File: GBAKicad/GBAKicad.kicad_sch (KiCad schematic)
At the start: 60 parts, among them J1 USB_C_Receptacle_USB2.0_16P, J2 Micro_SD_Card_Det1, J3 AudioJack3_SwitchT, SW1 SW_Push, SW10 SW_Push, SW11 SW_SPDT, SW2 SW_Push, SW3 SW_Push, SW4 SW_Push, SW5 SW_Push, SW6 SW_Push, SW7 SW_Push, SW8 SW_Push, SW9 SW_Push, U1 TFT_320x240, U2 XC6220B331MR, U3 TP4056-42-ESOP8, U4 MAX17048, U5 PCM5102A, U6 TPA2012D2RTJR, U7 ESP32-S3

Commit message: schemtics
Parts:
- removed C1, C2, C3, C4, C5, C6, C7, C8: 100nF, symbol Device:C
- removed C9: 1uF, symbol Device:C
- added C13, C14: 2.2uF, symbol Device:C
- added C15, C16, C17, C18, C19, C20, C21, C22, C24, C25: 100nF, symbol Device:C
- added C23: 1uF, symbol Device:C
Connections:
- net +3V3: now also C15.1, C16.1, C17.1, C18.1, C19.1, C20.2, C21.1, C22.2, C23.2; no longer U1.1 (VCC), U2.3 (CE), U2.5 (VOUT), U4.3 (VDD), U5.20 (DVDD), U5.8 (AVDD), U6.13 (PVDD), U6.3 (PVDD), U7.2 (VDD3P3), U7.20 (VDD3P3_RTC), U7.3 (VDD3P3), U7.46 (VDD3P3_CPU)
- net GND: now also C13.2, C14.2
- net VBAT: now also U2.3 (CE)
- net VBUS: now also C24.2, C25.1; no longer J1.A4 (VBUS), J1.A9 (VBUS), J1.B4 (VBUS), J1.B9 (VBUS), U3.4 (V_{CC})
- net at U5.18 (LDOO): now also C13.1
- net at U5.5 (VNEG): now also C14.1
- new net: C23.1, U2.5 (VOUT)
- new net: C21.2, U4.3 (VDD)
- new net: C22.1, U1.1 (VCC)
- new net: C18.2, U5.20 (DVDD)
- new net: C25.2, U3.4 (V_{CC})
- new net: C19.2, U5.8 (AVDD)
- new net: C24.1, J1.A4 (VBUS), J1.A9 (VBUS), J1.B4 (VBUS), J1.B9 (VBUS)
- new net: C17.2, U7.46 (VDD3P3_CPU)
- new net: C16.2, U7.20 (VDD3P3_RTC)
- new net: C15.2, U7.2 (VDD3P3), U7.3 (VDD3P3)
- new net PVDD: C20.1, U6.13 (PVDD), U6.3 (PVDD)
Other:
- moved on the sheet: BT1, C10, C11, C12, J1, J2, J3, LS1, R1, R10, R13, R14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

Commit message: schematics finshed???
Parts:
- removed C10, C11: 100nF, symbol Device:C
- added C26, C27: 100nF, Capacitor_SMD:C_0402_1005Metric, symbol Device:C
- BT1: footprint (none) -> Connector_JST:JST_PH_B2B-PH-K_1x02_P2.00mm_Vertical
- C12, C15, C16, C17, C18, C19, C20, C21, C22, C23, C24, C25: footprint (none) -> Capacitor_SMD:C_0402_1005Metric
- C13, C14: footprint (none) -> Capacitor_SMD:C_0201_0603Metric
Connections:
- net +3V3: now also C26.1, C27.1; no longer U7.29 (VDD_SPI), U7.55 (VDDA), U7.56 (VDDA)
- new net: C26.2, U7.55 (VDDA), U7.56 (VDDA)
- new net: C27.2, U7.29 (VDD_SPI)

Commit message: schemtics asign fotpitn pt 1
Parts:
- J1: footprint (none) -> Connector_USB:USB_C_Receptacle_HRO_TYPE-C-31-M-12
- J2: footprint (none) -> Connector_Card:microSD_HC_Hirose_DM3AT-SF-PEJM5
- J3: footprint (none) -> Connector_Audio:Jack_3.5mm_QingPu_WQP-PJ398SM_Vertical_CircularHoles
- LS1: footprint (none) -> Connector_JST:JST_PH_B2B-PH-K_1x02_P2.00mm_Vertical
- R1, R10, R11, R12, R13, R14, R15, R2, R3, R4, R5, R6, R7, R8, R9: footprint (none) -> Resistor_SMD:R_0402_1005Metric
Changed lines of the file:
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@@
 			)
 		)
-		(property "Footprint" ""
+		(property "Footprint" "Resistor_SMD:R_0402_1005Metric"
 			(at 222.25 244.602 90)
 			(hide yes)
@@
 			)
 		)
-		(property "Footprint" ""
+		(property "Footprint" "Resistor_SMD:R_0402_1005Metric"
 			(at 84.582 185.42 90)
 			(hide yes)
@@
 			)
 		)
-		(property "Footprint" ""
+		(property "Footprint" "Resistor_SMD:R_0402_1005Metric"
 			(at 304.8 94.488 90)
 			(hide yes)
@@
 			)
 		)
-		(property "Footprint" ""
+		(property "Footprint" "Resistor_SMD:R_0402_1005Metric"
 			(at 36.322 146.05 90)
 			(hide yes)
@@
 			)
 		)
-		(property "Footprint" ""
+		(property "Footprint" "Resistor_SMD:R_0402_1005Metric"
 			(at 304.8 76.708 90)
 			(hide yes)
@@
 			)
 		)
-		(property "Footprint" ""
+		(property "Footprint" "Resistor_SMD:R_0402_1005Metric"
 			(at 127.762 185.42 90)
 			(hide yes)
@@
 			)
 		)
-		(property "Footprint" ""
+		(property "Footprint" "Resistor_SMD:R_0402_1005Metric"
 			(at 127.762 146.05 90)
 			(hide yes)
@@
 			)
 		)
-		(property "Footprint" ""
+		(property "Footprint" "Resistor_SMD:R_0402_1005Metric"
 			(at 84.582 146.05 90)
 			(hide yes)
@@
 			)
 		)
-		(property "Footprint" ""
+		(property "Footprint" "Resistor_SMD:R_0402_1005Metric"
 			(at 389.89 178.562 90)
 			(hide yes)
@@
 			)
 		)
-		(property "Footprint" ""
+		(property "Footprint" "Resistor_SMD:R_0402_1005Metric"
 			(at 106.172 146.05 90)
 			(hide yes)
@@
 			)
 		)
-		(property "Footprint" ""
+		(property "Footprint" "Resistor_SMD:R_0402_1005Metric"
 			(at 106.172 185.42 90)
 			(hide yes)
@@
 			)
 		)
-		(property "Footprint" ""
+		(property "Footprint" "Connector_Audio:Jack_3.5mm_QingPu_WQP-PJ398SM_Vertical_CircularHoles"
 			(at 381 168.91 0)
 			(hide yes)
@@
 			)
 		)
-		(property "Footprint" ""
+		(property "Footprint" "Resistor_SMD:R_0402_1005Metric"
 			(at 36.322 185.42 90)
 			(hide yes)
@@
 			)
 		)
-		(property "Footprint" ""
+		(property "Footprint" "Resistor_SMD:R_0402_1005Metric"
 			(at 60.452 146.05 90)
 			(hide yes)
@@
 			)
 		)
-		(property "Footprint" ""
+		(property "Footprint" "Connector_JST:JST_PH_B2B-PH-K_1x02_P2.00mm_Vertical"
 			(at 361.95 180.34 0)
 			(hide yes)
@@
 			)
 		)
-		(property "Footprint" ""
+		(property "Footprint" "Resistor_SMD:R_0402_1005Metric"
 			(at 60.452 185.42 90)
 			(hide yes)
@@
 			)
 		)
-		(property "Footprint" ""
+		(property "Footprint" "Connector_Card:microSD_HC_Hirose_DM3AT-SF-PEJM5"
 			(at 387.35 67.31 0)
 			(hide yes)
@@
 			)
 		)
-		(property "Footprint" ""
+		(property "Footprint" "Resistor_SMD:R_0402_1005Metric"
 			(at 222.25 242.062 90)
 			(hide yes)
@@
 			)
 		)
-		(property "Footprint" ""
+		(property "Footprint" "Connector_USB:USB_C_Receptacle_HRO_TYPE-C-31-M-12"
 			(at 102.87 54.61 0)
 			(hide yes)

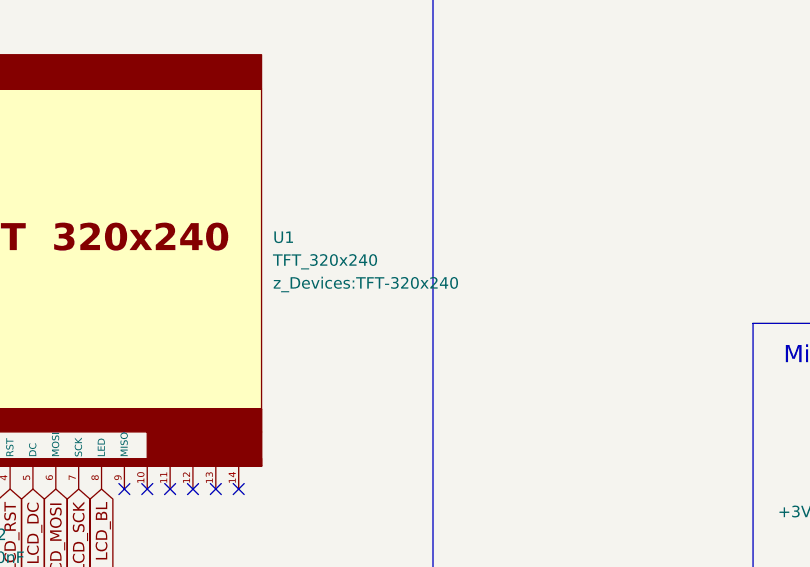
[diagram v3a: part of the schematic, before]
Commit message: schemtic assgining footpritns
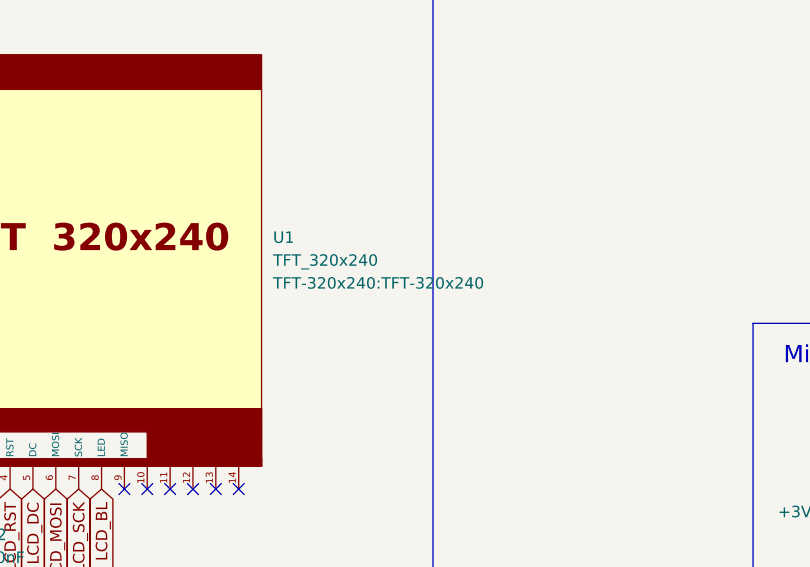
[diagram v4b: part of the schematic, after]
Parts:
- C12, C15, C16, C17, C18, C19, C20, C21, C22, C23, C24, C25, C26, C27: footprint Capacitor_SMD:C_0402_1005Metric -> Capacitor_SMD:C_0603_1608Metric
- C13, C14: footprint Capacitor_SMD:C_0201_0603Metric -> Capacitor_SMD:C_0603_1608Metric
- R1, R10, R11, R12, R13, R14, R15, R2, R3, R4, R5, R6, R7, R8, R9: footprint Resistor_SMD:R_0402_1005Metric -> Resistor_SMD:R_0603_1608Metric
- R16, R17, R18, R19, R20, R21, R22, R23, R24, R25: footprint (none) -> Resistor_SMD:R_0603_1608Metric
- SW1, SW10, SW2, SW3, SW4, SW5, SW6, SW7, SW8, SW9: footprint (none) -> Button_Switch_THT:SW_PUSH_6mm_H5mm
- SW11: footprint (none) -> Connector_PinHeader_2.54mm:PinHeader_1x14_P2.54mm_Vertical
- U1: footprint z_Devices:TFT-320x240 -> TFT-320x240:TFT-320x240
- U7: footprint Package_DFN_QFN:QFN-56-1EP_7x7mm_P0.4mm_EP4x4mm -> RF_Module:ESP32-S3-WROOM-1
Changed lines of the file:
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@@
 			)
 		)
-		(property "Footprint" "Capacitor_SMD:C_0402_1005Metric"
+		(property "Footprint" "Capacitor_SMD:C_0603_1608Metric"
 			(at 175.26 237.7948 0)
 			(hide yes)
@@
 			)
 		)
-		(property "Footprint" ""
+		(property "Footprint" "Button_Switch_THT:SW_PUSH_6mm_H5mm"
 			(at 91.44 157.48 0)
 			(hide yes)
@@
 			)
 		)
-		(property "Footprint" ""
+		(property "Footprint" "Button_Switch_THT:SW_PUSH_6mm_H5mm"
 			(at 67.31 157.48 0)
 			(hide yes)
@@
 			)
 		)
-		(property "Footprint" "Resistor_SMD:R_0402_1005Metric"
+		(property "Footprint" "Resistor_SMD:R_0603_1608Metric"
 			(at 222.25 244.602 90)
 			(hide yes)
@@
 			)
 		)
-		(property "Footprint" ""
+		(property "Footprint" "Resistor_SMD:R_0603_1608Metric"
 			(at 119.38 45.212 90)
 			(hide yes)
@@
 			)
 		)
-		(property "Footprint" ""
+		(property "Footprint" "Button_Switch_THT:SW_PUSH_6mm_H5mm"
 			(at 113.03 157.48 0)
 			(hide yes)
@@
 			)
 		)
-		(property "Footprint" "Resistor_SMD:R_0402_1005Metric"
+		(property "Footprint" "Resistor_SMD:R_0603_1608Metric"
 			(at 84.582 185.42 90)
 			(hide yes)
@@
 			)
 		)
-		(property "Footprint" "Resistor_SMD:R_0402_1005Metric"
+		(property "Footprint" "Resistor_SMD:R_0603_1608Metric"
 			(at 304.8 94.488 90)
 			(hide yes)
@@
 			)
 		)
-		(property "Footprint" ""
+		(property "Footprint" "Resistor_SMD:R_0603_1608Metric"
 			(at 226.06 169.418 90)
 			(hide yes)
@@
 			)
 		)
-		(property "Footprint" "Resistor_SMD:R_0402_1005Metric"
+		(property "Footprint" "Resistor_SMD:R_0603_1608Metric"
 			(at 36.322 146.05 90)
 			(hide yes)
@@
 			)
 		)
-		(property "Footprint" "Resistor_SMD:R_0402_1005Metric"
+		(property "Footprint" "Resistor_SMD:R_0603_1608Metric"
 			(at 304.8 76.708 90)
 			(hide yes)
@@
 			)
 		)
-		(property "Footprint" "Capacitor_SMD:C_0402_1005Metric"
+		(property "Footprint" "Capacitor_SMD:C_0603_1608Metric"
 			(at 192.7352 82.55 0)
 			(hide yes)
@@
 			)
 		)
-		(property "Footprint" ""
+		(property "Footprint" "Resistor_SMD:R_0603_1608Metric"
 			(at 170.18 141.478 90)
 			(hide yes)
@@
 			)
 		)
-		(property "Footprint" "Resistor_SMD:R_0402_1005Metric"
+		(property "Footprint" "Resistor_SMD:R_0603_1608Metric"
 			(at 127.762 185.42 90)
 			(hide yes)
@@
 			)
 		)
-		(property "Footprint" "Capacitor_SMD:C_0402_1005Metric"
+		(property "Footprint" "Capacitor_SMD:C_0603_1608Metric"
 			(at 272.7452 144.78 0)
 			(hide yes)
@@
 			)
 		)
-		(property "Footprint" "Capacitor_SMD:C_0402_1005Metric"
+		(property "Footprint" "Capacitor_SMD:C_0603_1608Metric"
 			(at 207.9752 228.6 0)
 			(hide yes)
@@
 			)
 		)
-		(property "Footprint" "Resistor_SMD:R_0402_1005Metric"
+		(property "Footprint" "Resistor_SMD:R_0603_1608Metric"
 			(at 127.762 146.05 90)
 			(hide yes)
@@
 			)
 		)
-		(property "Footprint" "Resistor_SMD:R_0402_1005Metric"
+		(property "Footprint" "Resistor_SMD:R_0603_1608Metric"
 			(at 84.582 146.05 90)
 			(hide yes)
@@
 			)
 		)
-		(property "Footprint" "Capacitor_SMD:C_0402_1005Metric"
+		(property "Footprint" "Capacitor_SMD:C_0603_1608Metric"
 			(at 275.2852 151.13 0)
 			(hide yes)
@@
 			)
 		)
-		(property "Footprint" ""
+		(property "Footprint" "Resistor_SMD:R_0603_1608Metric"
 			(at 191.77 245.618 90)
 			(hide yes)
@@
 			)
 		)
-		(property "Footprint" ""
+		(property "Footprint" "Resistor_SMD:R_0603_1608Metric"
 			(at 226.06 196.342 90)
 			(hide yes)
@@
 			)
 		)
-		(property "Footprint" "Resistor_SMD:R_0402_1005Metric"
+		(property "Footprint" "Resistor_SMD:R_0603_1608Metric"
 			(at 389.89 178.562 90)
 			(hide yes)
@@
 			)
 		)
-		(property "Footprint" ""
+		(property "Footprint" "Button_Switch_THT:SW_PUSH_6mm_H5mm"
 			(at 67.31 196.85 0)
 			(hide yes)
@@
 			)
 		)
-		(property "Footprint" "Resistor_SMD:R_0402_1005Metric"
+		(property "Footprint" "Resistor_SMD:R_0603_1608Metric"
 			(at 106.172 146.05 90)
 			(hide yes)
@@
 			)
 		)
-		(property "Footprint" "Resistor_SMD:R_0402_1005Metric"
+		(property "Footprint" "Resistor_SMD:R_0603_1608Metric"
 			(at 106.172 185.42 90)
 			(hide yes)
@@
 			)
 		)
-		(property "Footprint" "Capacitor_SMD:C_0402_1005Metric"
+		(property "Footprint" "Capacitor_SMD:C_0603_1608Metric"
 			(at 123.19 38.4048 0)
 			(hide yes)
@@
 			)
 		)
-		(property "Footprint" "Capacitor_SMD:C_0402_1005Metric"
+		(property "Footprint" "Capacitor_SMD:C_0603_1608Metric"
 			(at 358.14 161.5948 0)
 			(hide yes)
@@
 			)
 		)
-		(property "Footprint" ""
+		(property "Footprint" "Connector_PinHeader_2.54mm:PinHeader_1x14_P2.54mm_Vertical"
 			(at 229.87 266.7 0)
 			(hide yes)
@@
 			)
 		)
-		(property "Footprint" ""
+		(property "Footprint" "Button_Switch_THT:SW_PUSH_6mm_H5mm"
 			(at 134.62 196.85 0)
 			(hide yes)
@@
 			)
 		)
-		(property "Footprint" "Resistor_SMD:R_0402_1005Metric"
+		(property "Footprint" "Resistor_SMD:R_0603_1608Metric"
 			(at 36.322 185.42 90)
 			(hide yes)
@@
 			)
 		)
-		(property "Footprint" ""
+		(property "Footprint" "Button_Switch_THT:SW_PUSH_6mm_H5mm"
 			(at 113.03 196.85 0)
 			(hide yes)
@@
 			)
 		)
-		(property "Footprint" "Resistor_SMD:R_0402_1005Metric"
+		(property "Footprint" "Resistor_SMD:R_0603_1608Metric"
 			(at 60.452 146.05 90)
 			(hide yes)
@@
 			)
 		)
-		(property "Footprint" ""
+		(property "Footprint" "Resistor_SMD:R_0603_1608Metric"
 			(at 297.18 239.522 90)
 			(hide yes)
@@
 			)
 		)
-		(property "Footprint" "Capacitor_SMD:C_0402_1005Metric"
+		(property "Footprint" "Capacitor_SMD:C_0603_1608Metric"
 			(at 204.1652 130.81 0)
 			(hide yes)
@@
 			)
 		)
-		(property "Footprint" "Capacitor_SMD:C_0402_1005Metric"
+		(property "Footprint" "Capacitor_SMD:C_0603_1608Metric"
 			(at 194.0052 130.81 0)
 			(hide yes)
@@
 			)
 		)
-		(property "Footprint" ""
+		(property "Footprint" "Resistor_SMD:R_0603_1608Metric"
 			(at 271.78 234.442 90)
 			(hide yes)
@@
 			)
 		)
-		(property "Footprint" "Capacitor_SMD:C_0402_1005Metric"
+		(property "Footprint" "Capacitor_SMD:C_0603_1608Metric"
 			(at 247.65 235.2548 0)
 			(hide yes)
@@
 			)
 		)
-		(property "Footprint" "Capacitor_SMD:C_0402_1005Metric"
+		(property "Footprint" "Capacitor_SMD:C_0603_1608Metric"
 			(at 199.0852 129.54 0)
 			(hide yes)
@@
 			)
 		)
-		(property "Footprint" ""
+		(property "Footprint" "Resistor_SMD:R_0603_1608Metric"
 			(at 191.77 248.158 90)
 			(hide yes)
@@
 			)
 		)
-		(property "Footprint" "Resistor_SMD:R_0402_1005Metric"
+		(property "Footprint" "Resistor_SMD:R_0603_1608Metric"
 			(at 60.452 185.42 90)
 			(hide yes)
@@
 			)
 		)
-		(property "Footprint" "Capacitor_SMD:C_0402_1005Metric"
+		(property "Footprint" "Capacitor_SMD:C_0603_1608Metric"
 			(at 196.5452 124.46 0)
 			(hide yes)
@@
 			)
 		)
-		(property "Footprint" ""
+		(property "Footprint" "Button_Switch_THT:SW_PUSH_6mm_H5mm"
 			(at 91.44 196.85 0)
 			(hide yes)
@@
 			)
 		)
-		(property "Footprint" "Capacitor_SMD:C_0402_1005Metric"
+		(property "Footprint" "Capacitor_SMD:C_0603_1608Metric"
 			(at 286.7152 177.8 0)
 			(hide yes)
@@
 			)
 		)
-		(property "Footprint" ""
+		(property "Footprint" "Button_Switch_THT:SW_PUSH_6mm_H5mm"
 			(at 43.18 157.48 0)
 			(hide yes)
@@
 			)
 		)
-		(property "Footprint" "Package_DFN_QFN:QFN-56-1EP_7x7mm_P0.4mm_EP4x4mm"
+		(property "Footprint" "RF_Module:ESP32-S3-WROOM-1"
 			(at 198.12 218.44 0)
 			(hide yes)
@@
 			)
 		)
-		(property "Footprint" "Capacitor_SMD:C_0201_0603Metric"
+		(property "Footprint" "Capacitor_SMD:C_0603_1608Metric"
 			(at 302.26 181.9148 0)
 			(hide yes)
@@
 			)
 		)
-		(property "Footprint" "Capacitor_SMD:C_0402_1005Metric"
+		(property "Footprint" "Capacitor_SMD:C_0603_1608Metric"
 			(at 201.6252 116.84 0)
 			(hide yes)
@@
 			)
 		)
-		(property "Footprint" "Resistor_SMD:R_0402_1005Metric"
+		(property "Footprint" "Resistor_SMD:R_0603_1608Metric"
 			(at 222.25 242.062 90)
 			(hide yes)
@@
 			)
 		)
-		(property "Footprint" ""
+		(property "Footprint" "Button_Switch_THT:SW_PUSH_6mm_H5mm"
 			(at 43.18 196.85 0)
 			(hide yes)
@@
 			)
 		)
-		(property "Footprint" ""
+		(property "Footprint" "Button_Switch_THT:SW_PUSH_6mm_H5mm"
 			(at 134.62 157.48 0)
 			(hide yes)
@@
 			)
 		)
-		(property "Footprint" ""
+		(property "Footprint" "Resistor_SMD:R_0603_1608Metric"
 			(at 297.18 242.062 90)
 			(hide yes)
@@
 			)
 		)
-		(property "Footprint" ""
+		(property "Footprint" "Resistor_SMD:R_0603_1608Metric"
 			(at 119.38 42.672 90)
 			(hide yes)
@@
 			)
 		)
-		(property "Footprint" "z_Devices:TFT-320x240"
+		(property "Footprint" "TFT-320x240:TFT-320x240"
 			(at 228.6 49.5299 0)
 			(show_name no)
@@
 			)
 		)
-		(property "Footprint" "Capacitor_SMD:C_0201_0603Metric"
+		(property "Footprint" "Capacitor_SMD:C_0603_1608Metric"
 			(at 293.37 184.4548 0)
 			(hide yes)

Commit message: Schematics done!
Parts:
- removed BT1: Battery, Connector_JST:JST_PH_B2B-PH-K_1x02_P2.00mm_Vertical, symbol Device:Battery
- removed C12, C23: 1uF, Capacitor_SMD:C_0603_1608Metric, symbol Device:C
- removed C14: 2.2uF, Capacitor_SMD:C_0603_1608Metric, symbol Device:C
- removed C15, C16, C17, C18, C19, C20, C21, C22, C24, C25, C26, C27: 100nF, Capacitor_SMD:C_0603_1608Metric, symbol Device:C
- removed J2: Micro_SD_Card_Det1, Connector_Card:microSD_HC_Hirose_DM3AT-SF-PEJM5, symbol Connector:Micro_SD_Card_Det1
- removed J3: AudioJack3_SwitchT, Connector_Audio:Jack_3.5mm_QingPu_WQP-PJ398SM_Vertical_CircularHoles, symbol Connector_Audio:AudioJack3_SwitchT
- removed LS1: Speaker, Connector_JST:JST_PH_B2B-PH-K_1x02_P2.00mm_Vertical, symbol Device:Speaker
- removed R18, R21, R23: 10k, Resistor_SMD:R_0603_1608Metric, symbol Device:R
- removed R19, R20: 4.7k, Resistor_SMD:R_0603_1608Metric, symbol Device:R
- removed R22, R25: 5.1k, Resistor_SMD:R_0603_1608Metric, symbol Device:R
- removed R24: 100, Resistor_SMD:R_0603_1608Metric, symbol Device:R
- removed SW11: SW_SPDT, Connector_PinHeader_2.54mm:PinHeader_1x14_P2.54mm_Vertical, symbol Switch:SW_SPDT
- removed SW2: SW_Push, Button_Switch_THT:SW_PUSH_6mm_H5mm, symbol Switch:SW_Push
- removed U1: TFT_320x240, TFT-320x240:TFT-320x240, symbol tft_320x240:TFT_320x240
- removed U2: XC6220B331MR, Package_TO_SOT_SMD:SOT-23-5, symbol Regulator_Linear:XC6220B331MR
- removed U4: MAX17048, Package_DFN_QFN:DFN-8-1EP_2x2mm_P0.5mm_EP0.7x1.3mm, symbol PCM_marbastlib-various:MAX17048
- removed U5: PCM5102A, Package_SO:TSSOP-20_4.4x6.5mm_P0.65mm, symbol Audio:PCM5102A
- removed U6: TPA2012D2RTJR, TPA2012D2RTJR:QFN50P400X400X80-21N270X270, symbol TPA2012D2RTJR:TPA2012D2RTJR
- removed U7: ESP32-S3, RF_Module:ESP32-S3-WROOM-1, symbol MCU_Espressif:ESP32-S3
- added C1, C3: 100nF, Capacitor_SMD:C_0603_1608Metric, symbol Device:C
- added C10, C4, C5, C6: 10uF, Capacitor_SMD:C_0603_1608Metric, symbol Device:C
- added C11: 10uF, Capacitor_Tantalum_SMD:CP_EIA-3216-18_Kemet-A, symbol Device:C_Polarized
- added C12: 22uF, Capacitor_Tantalum_SMD:CP_EIA-3216-18_Kemet-A, symbol Device:C_Polarized
- added C2: 22nF, Capacitor_SMD:C_0603_1608Metric, symbol Device:C
- added C7, C8, C9: 100uF, Capacitor_SMD:C_0603_1608Metric, symbol Device:C
- added D1: RED, LED_SMD:LED_0603_1608Metric, symbol Device:LED
- added D2: BLUE, LED_SMD:LED_0603_1608Metric, symbol Device:LED
- added J2: BATT_Conn, symbol Connector:Conn_01x02_Socket
- added J3: Jumper, symbol Jumper:SolderJumper_2_Open
- added J4: OLED_Conn, symbol Connector:Conn_01x04_Socket
- added Q1: (no value), Custom Footprints:SOT-23-6L_TCP, symbol DIY_symbols:FS8205A
- added Q2: PMOS, symbol Simulation_SPICE:PMOS
- added SW11, SW12, SW13, SW14, SW15: SW_Push, symbol Switch:SW_Push
- added SW16: BTN_SYS, symbol Switch:SW_Push
- added SW2: SW_SPDT, symbol Switch:SW_SPDT
- added TP1, TP3, TP5: TestPoint, symbol Connector:TestPoint
- added TP4: AMS_3V3, symbol Connector:TestPoint
- added U1: ESP32-S3-WROOM-1, RF_Module:ESP32-S3-WROOM-1, symbol RF_Module:ESP32-S3-WROOM-1
- added U2: MIC5219-3.3YM5, Package_TO_SOT_SMD:SOT-23-5, symbol Regulator_Linear:MIC5219-3.3YM5
- added U4: DW01A, Package_TO_SOT_SMD:SOT-23-6, symbol Battery_Management:DW01A
- added U5: AMS1117-3.3, Package_TO_SOT_SMD:SOT-223-3_TabPin2, symbol Regulator_Linear:AMS1117-3.3
- C13: value 2.2uF -> 100nF
- J1: footprint Connector_USB:USB_C_Receptacle_HRO_TYPE-C-31-M-12 -> Connector_USB:USB_C_Receptacle_GCT_USB4105-xx-A_16P_TopMnt_Horizontal
- R1, R17: footprint Resistor_SMD:R_0603_1608Metric -> (none)
- R10, R11, R12, R13, R15, R16: value 10k -> 100k; footprint Resistor_SMD:R_0603_1608Metric -> (none)
- R14: value 1.2k -> 100k; footprint Resistor_SMD:R_0603_1608Metric -> (none)
- R2, R3: value 10k -> 5.1k; footprint Resistor_SMD:R_0603_1608Metric -> (none)
- R4: value 10k -> 1.2k; footprint Resistor_SMD:R_0603_1608Metric -> (none)
- R5, R6, R7: value 10k -> 1k; footprint Resistor_SMD:R_0603_1608Metric -> (none)
- R8, R9: value 10k -> 100R; footprint Resistor_SMD:R_0603_1608Metric -> (none)
- SW1: value SW_Push -> EN; footprint Button_Switch_THT:SW_PUSH_6mm_H5mm -> (none)
- SW10, SW4, SW5, SW6, SW7, SW8, SW9: footprint Button_Switch_THT:SW_PUSH_6mm_H5mm -> (none)
- SW3: value SW_Push -> BOOT; footprint Button_Switch_THT:SW_PUSH_6mm_H5mm -> (none)
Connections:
- net D_DOWN is gone; now on net GND: R4.2, SW4.1
- net D_LEFT is gone; now on net GND: R2.2
- net +3V3: now also C1.2, C12.1, C2.2, J3.2 (B), J4.2 (Pin_2), Q2.1 (D), TP4.1, U1.2 (3V3), U5.2 (VO); no longer R10.1, R11.1, R12.1, R13.1, R15.1, R16.1, R17.1, R2.1, R3.1, R4.1, R5.1, R6.1, R7.1, R8.1, R9.1, U3.8 (CE)
- net BTN_A: now also SW12.2, U1.38 (IO2); no longer R5.2, SW5.1
- net BTN_B: now also SW13.2, U1.6 (IO6); no longer R6.2, SW6.1
- net BTN_L: now also SW4.2, U1.18 (IO10); no longer R9.2, SW9.1
- net BTN_R: now also SW10.2, U1.39 (IO1); no longer R10.2, SW10.1
- net BTN_SELECT: now also SW15.2, U1.7 (IO7); no longer R7.2, SW7.1
- net BTN_START: now also SW9.2, U1.10 (IO17); no longer R8.2, SW8.1
- net GND: now also R11.2, R13.2, R16.2, R3.2, R7.2, SW10.1, SW5.1, SW6.1, SW7.1, SW8.1, SW9.1, U3.1 (TEMP), C1.1, C10.2, C11.2, C12.2, C2.1, C3.2, C4.2, C5.2, C6.2, C7.2, C8.2, J4.1 (Pin_1), Q1.1 (S1), SW11.1, SW12.1, SW13.1, SW14.1, SW15.1, SW16.1, SW2.3 (C), TP3.1, U1.1 (GND), U1.40 (GND), U1.41 (GND), U2.2 (GND), U5.1 (GND); no longer R14.1, SW10.2, SW4.2, SW5.2, SW6.2, SW7.2, SW8.2, SW9.2, U3.9 (EPAD)
- net at R14.2: now also C6.1, C7.1, J3.1 (A), Q2.3 (S), TP5.1, U2.5 (OUT); no longer U3.2 (PROG)
- net at J1.B5 (CC2): now also R3.1
- net BATT_CHECK: now reaches R12.2
- net BATT_CHECK: now also C13.1, R13.1
- net +5V: now reaches U3.4 (V_{CC})
- net +5V: now also J1.A4 (VBUS), J1.A9 (VBUS), J1.B4 (VBUS), J1.B9 (VBUS), R10.1, R15.1, R5.1, R6.1, U3.8 (CE), C11.1, TP1.1, U5.3 (VI)
- net at U3.7 (~{CHRG}): now also D1.1 (K); no longer R16.2
- net at U3.6 (~{STDBY}): now also C8.1, D2.1 (K); no longer R17.2
- net at R15.2: now also R16.1, R17.2; no longer U3.1 (TEMP)
- net at J1.A5 (CC1): now also R2.1
- net D_RIGHT renamed EN
- net EN: now also C3.1, C4.1, U1.3 (EN)
- net D_UP: no longer names the net of SW3.1
- net D_UP: now also R9.2; no longer R3.2
- net USP_DM renamed Data-
- net Data-: now also U1.13 (USB_D-)
- net USP_DP renamed Data+
- net Data+: now also U1.14 (USB_D+)
- net VBAT renamed +BATT
- net +BATT: now also R12.1, R8.1, C10.1, J2.1 (Pin_1), SW2.1 (A)
- new net: C9.1, R8.2, U4.5 (VCC)
- new net: D1.2 (A), R5.2
- new net: Q1.4 (G2), U4.1 (OD)
- new net: Q1.6 (G1), U4.3 (OC)
- new net: D2.2 (A), R6.2
- new net: C5.1, SW2.2 (B), U2.1 (IN), U2.3 (EN)
- new net: Q2.2 (G), R14.1, R17.1
- new net: R4.1, U3.2 (PROG)
- new net: R7.1, U4.2 (CS)
- new net -BATT: C9.2, J2.2 (Pin_2), Q1.3 (S2), U4.6 (GND)
- new net BAT_CHECK: U1.4 (IO4)
- new net BOOT: R9.1, U1.27 (IO0)
- new net BTN_DOWN: SW7.2, U1.19 (IO11)
- new net BTN_LEFT: SW6.2, U1.20 (IO12)
- new net BTN_RIGHT: SW8.2, U1.21 (IO13)
- new net BTN_SYS: SW16.2
- new net BTN_Sys: U1.33 (IO40)
- new net BTN_UP: SW5.2, U1.11 (IO18)
- new net BTN_X: SW11.2, SW14.2, U1.31 (IO38)
- new net BTN_Y: U1.22 (IO14)
- new net CHRG_CHECK: R10.2, R11.1, U1.5 (IO5)
- new net OLED_SCK: J4.3 (Pin_3), U1.17 (IO9)
- new net OLED_SDA: J4.4 (Pin_4), U1.12 (IO8)
- no-connect marks 31 -> 20
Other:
- note added: "Battery Charging and Protection"
- note added: "Double LDO Circuit"
- note added: "ESP32 and Hardware Buttons"
- note added: "Enable and Hard Reboot"
- note added: "GPIO Console Buttons"
- note added: "Peripherals"
- note removed: "Audio Chain"
- note removed: "Button Matrix"
- note removed: "ESP-32 S3"
- note removed: "ILI9341 Display"
- note removed: "MicroSD Slot"
- note removed: "Power!!!"
- note removed: "USB-C Port"
